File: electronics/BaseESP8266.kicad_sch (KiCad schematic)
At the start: 15 parts, among them P3 CONN_01X09, P4 CONN_01X09, SW1 Reset, T1 CONN_01X01, T2 CONN_01X01, U4 ESP-13-WROOM-02

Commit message: revisions on PCB
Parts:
- D1, D2: Farnell Price/Stock https://uk.farnell.com/wurth-elektronik/155124vs73200/led-1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 -> https://uk.farnell.com/multicomp-pro/mp008279/led-green-70m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
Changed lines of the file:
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@@
-(kicad_sch (version 20221110) (generator eeschema)
+(kicad_sch (version 20230121) (generator eeschema)
   (paper "A4")
   (junction (at 144.78 57.15) (diameter 0) (color 0 0 0 0)
@@
       (project "MyBikesGotLED"
         (path "/ea56fda8-6f8e-4826-a040-5c9b3e8e5cfa/00000000-0000-0000-0000-00005f8dad46"
-          (reference "R17") (unit 1) (value "R10k") (footprint "Resistor_SMD:R_0603_1608Metric_Pad0.98x0.95mm_HandSolder")
+          (reference "R17") (unit 1)
         )
       )
@@
       (project "MyBikesGotLED"
         (path "/ea56fda8-6f8e-4826-a040-5c9b3e8e5cfa/00000000-0000-0000-0000-00005f8dad46"
-          (reference "T2") (unit 1) (value "CONN_01X01") (footprint "TestPoint:TestPoint_Pad_D2.0mm")
+          (reference "T2") (unit 1)
         )
       )
@@
       (project "MyBikesGotLED"
         (path "/ea56fda8-6f8e-4826-a040-5c9b3e8e5cfa/00000000-0000-0000-0000-00005f8dad46"
-          (reference "T1") (unit 1) (value "CONN_01X01") (footprint "TestPoint:TestPoint_Pad_D2.0mm")
+          (reference "T1") (unit 1)
         )
       )
@@
       (project "MyBikesGotLED"
         (path "/ea56fda8-6f8e-4826-a040-5c9b3e8e5cfa/00000000-0000-0000-0000-00005f8dad46"
-          (reference "C9") (unit 1) (value "C47nF") (footprint "Capacitor_SMD:C_0603_1608Metric_Pad1.08x0.95mm_HandSolder")
+          (reference "C9") (unit 1)
         )
       )
@@
       (project "MyBikesGotLED"
         (path "/ea56fda8-6f8e-4826-a040-5c9b3e8e5cfa/00000000-0000-0000-0000-00005f8dad46"
-          (reference "R12") (unit 1) (value "R560") (footprint "Resistor_SMD:R_0603_1608Metric_Pad0.98x0.95mm_HandSolder")
+          (reference "R12") (unit 1)
         )
       )
@@
       (project "MyBikesGotLED"
         (path "/ea56fda8-6f8e-4826-a040-5c9b3e8e5cfa/00000000-0000-0000-0000-00005f8dad46"
-          (reference "R16") (unit 1) (value "R560") (footprint "Resistor_SMD:R_0603_1608Metric_Pad0.98x0.95mm_HandSolder")
+          (reference "R16") (unit 1)
         )
       )
@@
       (project "MyBikesGotLED"
         (path "/ea56fda8-6f8e-4826-a040-5c9b3e8e5cfa/00000000-0000-0000-0000-00005f8dad46"
-          (reference "R15") (unit 1) (value "R560") (footprint "Resistor_SMD:R_0603_1608Metric_Pad0.98x0.95mm_HandSolder")
+          (reference "R15") (unit 1)
         )
       )
@@
       (effects (font (size 1.27 1.27)) hide)
     )
-    (property "Farnell Price/Stock" "https://uk.farnell.com/wurth-elektronik/155124vs73200/led-1204-b-green-50mcd-573nm/dp/2322102" (at 248.92 91.44 0)
-      (effects (font (size 1.27 1.27)) hide)
-    )
-    (pin "1")
-    (pin "2")
-    (instances
-      (project "MyBikesGotLED"
-        (path "/ea56fda8-6f8e-4826-a040-5c9b3e8e5cfa/00000000-0000-0000-0000-00005f8dad46"
-          (reference "D2") (unit 1) (value "LED") (footprint "LED_SMD:LED_0805_2012Metric_Pad1.15x1.40mm_HandSolder")
+    (property "Farnell Price/Stock" "https://uk.farnell.com/multicomp-pro/mp008279/led-green-70mcd-576nm-0805/dp/3796308" (at 248.92 91.44 0)
+      (effects (font (size 1.27 1.27)) hide)
+    )
+    (pin "1")
+    (pin "2")
+    (instances
+      (project "MyBikesGotLED"
+        (path "/ea56fda8-6f8e-4826-a040-5c9b3e8e5cfa/00000000-0000-0000-0000-00005f8dad46"
+          (reference "D2") (unit 1)
         )
       )
@@
       (effects (font (size 1.27 1.27)) hide)
     )
-    (property "Farnell Price/Stock" "https://uk.farnell.com/wurth-elektronik/155124vs73200/led-1204-b-green-50mcd-573nm/dp/2322102" (at 237.49 91.44 0)
-      (effects (font (size 1.27 1.27)) hide)
-    )
-    (pin "1")
-    (pin "2")
-    (instances
-      (project "MyBikesGotLED"
-        (path "/ea56fda8-6f8e-4826-a040-5c9b3e8e5cfa/00000000-0000-0000-0000-00005f8dad46"
-          (reference "D1") (unit 1) (value "LED") (footprint "LED_SMD:LED_0805_2012Metric_Pad1.15x1.40mm_HandSolder")
+    (property "Farnell Price/Stock" "https://uk.farnell.com/multicomp-pro/mp008279/led-green-70mcd-576nm-0805/dp/3796308" (at 237.49 91.44 0)
+      (effects (font (size 1.27 1.27)) hide)
+    )
+    (pin "1")
+    (pin "2")
+    (instances
+      (project "MyBikesGotLED"
+        (path "/ea56fda8-6f8e-4826-a040-5c9b3e8e5cfa/00000000-0000-0000-0000-00005f8dad46"
+          (reference "D1") (unit 1)
         )
       )
@@
       (project "MyBikesGotLED"
         (path "/ea56fda8-6f8e-4826-a040-5c9b3e8e5cfa/00000000-0000-0000-0000-00005f8dad46"
-          (reference "SW1") (unit 1) (value "Reset") (footprint "mcqn-kicad-lib:SW_SPST_GULLWING")
+          (reference "SW1") (unit 1)
         )
       )
@@
       (project "MyBikesGotLED"
         (path "/ea56fda8-6f8e-4826-a040-5c9b3e8e5cfa/00000000-0000-0000-0000-00005f8dad46"
-          (reference "P3") (unit 1) (value "CONN_01X09") (footprint "Connector_PinSocket_2.54mm:PinSocket_1x09_P2.54mm_Vertical")
+          (reference "P3") (unit 1)
         )
       )
@@
       (project "MyBikesGotLED"
         (path "/ea56fda8-6f8e-4826-a040-5c9b3e8e5cfa/00000000-0000-0000-0000-00005f8dad46"
-          (reference "P4") (unit 1) (value "CONN_01X09") (footprint "Connector_PinSocket_2.54mm:PinSocket_1x09_P2.54mm_Vertical")
+          (reference "P4") (unit 1)
         )
       )
@@
       (project "MyBikesGotLED"
         (path "/ea56fda8-6f8e-4826-a040-5c9b3e8e5cfa/00000000-0000-0000-0000-00005f8dad46"
-          (reference "R13") (unit 1) (value "R10k") (footprint "Resistor_SMD:R_0603_1608Metric_Pad0.98x0.95mm_HandSolder")
+          (reference "R13") (unit 1)
         )
       )
@@
       (project "MyBikesGotLED"
         (path "/ea56fda8-6f8e-4826-a040-5c9b3e8e5cfa/00000000-0000-0000-0000-00005f8dad46"
-          (reference "#PWR05") (unit 1) (value "+3V3") (footprint "")
+          (reference "#PWR05") (unit 1)
         )
       )
@@
       (project "MyBikesGotLED"
         (path "/ea56fda8-6f8e-4826-a040-5c9b3e8e5cfa/00000000-0000-0000-0000-00005f8dad46"
-          (reference "#PWR06") (unit 1) (value "GND") (footprint "")
+          (reference "#PWR06") (unit 1)
         )
       )
@@
       (project "MyBikesGotLED"
         (path "/ea56fda8-6f8e-4826-a040-5c9b3e8e5cfa/00000000-0000-0000-0000-00005f8dad46"
-          (reference "#PWR04") (unit 1) (value "GND") (footprint "")
+          (reference "#PWR04") (unit 1)
         )
       )
@@
       (project "MyBikesGotLED"
         (path "/ea56fda8-6f8e-4826-a040-5c9b3e8e5cfa/00000000-0000-0000-0000-00005f8dad46"
-          (reference "R14") (unit 1) (value "10k") (footprint "Resistor_SMD:R_0603_1608Metric_Pad0.98x0.95mm_HandSolder")
+          (reference "R14") (unit 1)
         )
       )
@@
       (project "MyBikesGotLED"
         (path "/ea56fda8-6f8e-4826-a040-5c9b3e8e5cfa/00000000-0000-0000-0000-00005f8dad46"
-          (reference "U4") (unit 1) (value "ESP-13-WROOM-02") (footprint "RF_Module:ESP-WROOM-02")
+          (reference "U4") (unit 1)
         )
       )
@@
       (project "MyBikesGotLED"
         (path "/ea56fda8-6f8e-4826-a040-5c9b3e8e5cfa/00000000-0000-0000-0000-00005f8dad46"
-          (reference "#PWR03") (unit 1) (value "+3V3") (footprint "")
-        )
-      )
+          (reference "#PWR03") (unit 1)
+        )
+      )

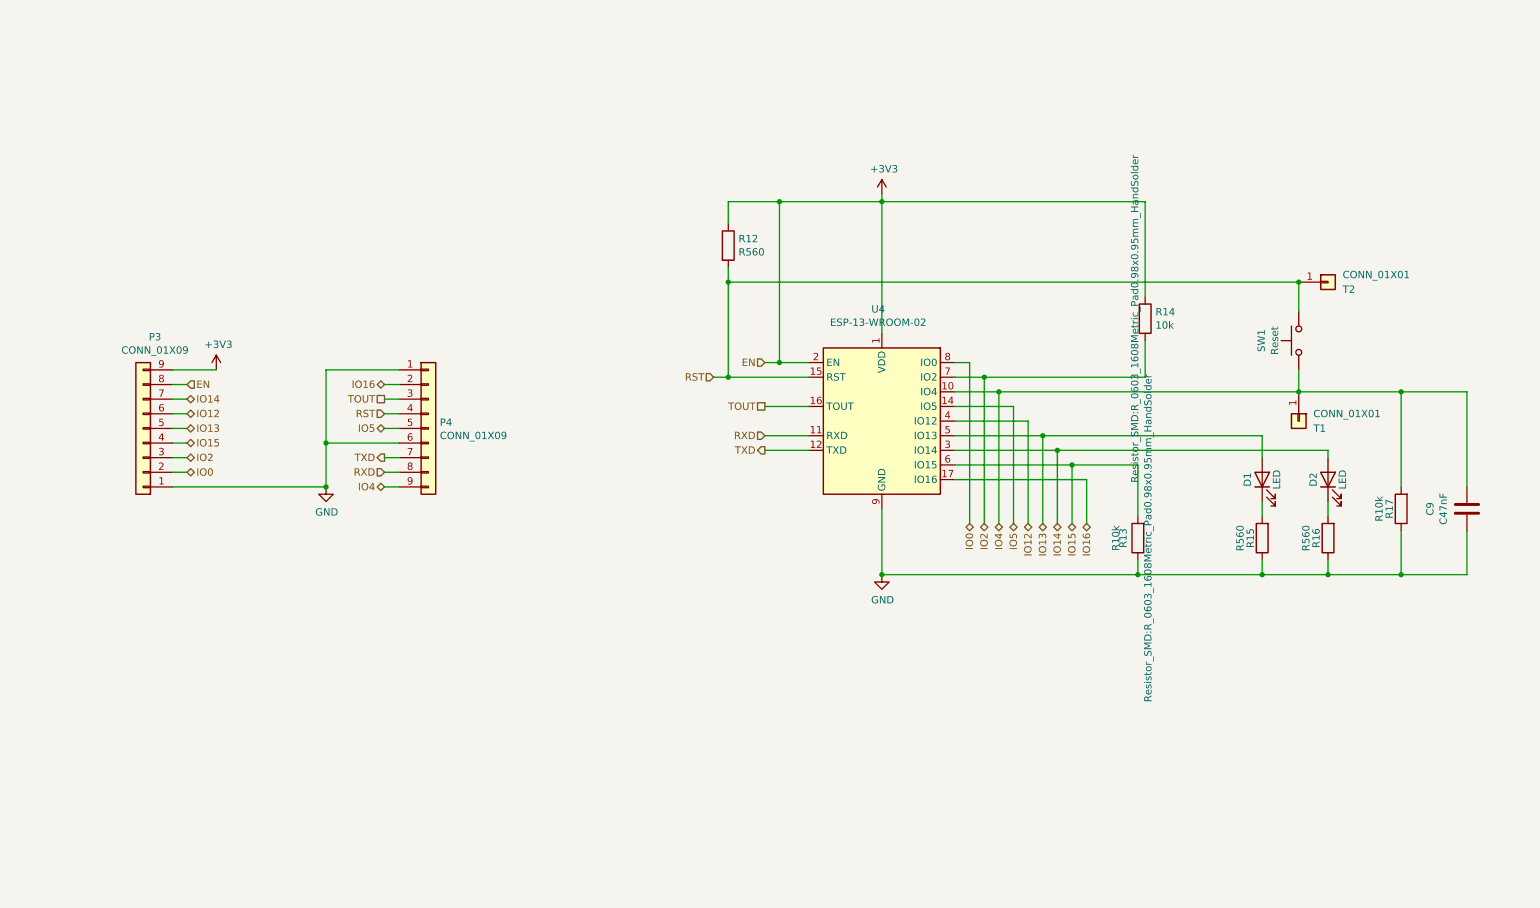
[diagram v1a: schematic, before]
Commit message: Swapped ESP8266 for ESP32, added BQ25895M battery management, and NX3DV42GU switch for d+/-
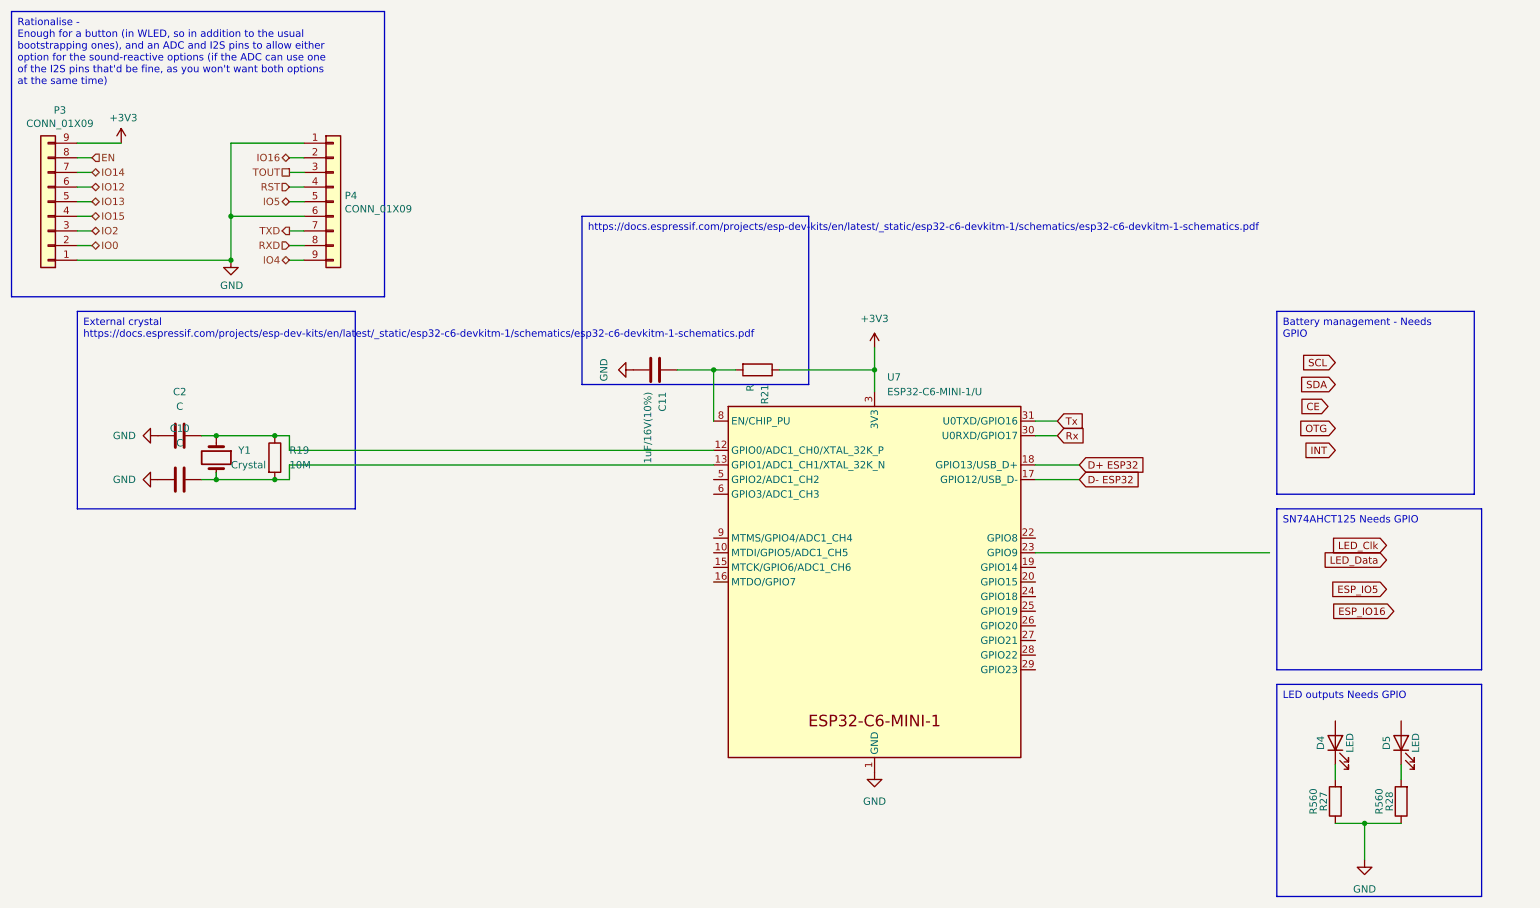
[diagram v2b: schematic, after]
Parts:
- removed C9: C47nF, Capacitor_SMD:C_0603_1608Metric_Pad1.08x0.95mm_HandSolder, symbol Device:C
- removed D1, D2: LED, LED_SMD:LED_0805_2012Metric_Pad1.15x1.40mm_HandSolder, symbol Device:LED
- removed R12, R15, R16: R560, Resistor_SMD:R_0603_1608Metric_Pad0.98x0.95mm_HandSolder, symbol Device:R
- removed R13, R17: R10k, Resistor_SMD:R_0603_1608Metric_Pad0.98x0.95mm_HandSolder, symbol Device:R
- removed R14: 10k, Resistor_SMD:R_0603_1608Metric_Pad0.98x0.95mm_HandSolder, symbol Device:R
- removed SW1: Reset, mcqn-kicad-lib:SW_SPST_GULLWING, symbol Switch:SW_Push
- removed T1, T2: CONN_01X01, TestPoint:TestPoint_Pad_D2.0mm, symbol Connector_Generic:Conn_01x01
- removed U4: ESP-13-WROOM-02, RF_Module:ESP-WROOM-02, symbol RF_Module:ESP-WROOM-02
- added C10, C2: C, symbol Device:C
- added C11: 1uF/16V(10%), symbol Device:C
- added D4, D5: LED, LED_SMD:LED_0805_2012Metric_Pad1.15x1.40mm_HandSolder, symbol Device:LED
- added R19: 10M, symbol Device:R
- added R21: R, symbol Device:R
- added R27, R28: R560, Resistor_SMD:R_0603_1608Metric_Pad0.98x0.95mm_HandSolder, symbol Device:R
- added U7: ESP32-C6-MINI-1/U, PCM_Espressif:ESP32-C6-MINI-1, symbol PCM_Espressif:ESP32-C6-MINI-1/U
- added Y1: Crystal, symbol Device:Crystal
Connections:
- net +3V3: now also R21.1, U7.3 (3V3); no longer P3.8 (Pin_8)
- net GND: now also C10.2, C11.2, C2.2, R27.1, R28.1, U7.1 (GND), U7.11 (GND), U7.14 (GND), U7.2 (GND), U7.36 (GND), U7.37 (GND), U7.38 (GND), U7.39 (GND), U7.40 (GND), U7.41 (GND), U7.42 (GND), U7.43 (GND), U7.44 (GND), U7.45 (GND), U7.46 (GND), U7.47 (GND), U7.48 (GND), U7.49 (GND), U7.50 (GND), U7.51 (GND), U7.52 (GND), U7.53 (GND)
- new net: C2.1, R19.1, U7.12 (GPIO0/ADC1_CH0/XTAL_32K_P), Y1.1
- new net: C10.1, R19.2, U7.13 (GPIO1/ADC1_CH1/XTAL_32K_N), Y1.2
- new net: C11.1, R21.2, U7.8 (EN/CHIP_PU)
- new net: D5.1 (K), R28.2
- new net: D4.1 (K), R27.2
- new net D+ ESP32: U7.18 (GPIO13/USB_D+)
- new net D- ESP32: U7.17 (GPIO12/USB_D-)
- new net EN: P3.8 (Pin_8)
- new net Rx: U7.30 (U0RXD/GPIO17)
- new net Tx: U7.31 (U0TXD/GPIO16)
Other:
- moved on the sheet: P3, P4
